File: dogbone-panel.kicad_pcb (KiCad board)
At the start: 2 copper layers, 35 x 60 mm, 72 parts, among them M1 THRU_HOLE_PAD, M10 THRU_HOLE_PAD, M11 THRU_HOLE_PAD, M12 THRU_HOLE_PAD, M2 THRU_HOLE_PAD, M3 THRU_HOLE_PAD, M4 THRU_HOLE_PAD, M5 THRU_HOLE_PAD, M6 THRU_HOLE_PAD, M7 THRU_HOLE_PAD, M8 THRU_HOLE_PAD, M9 THRU_HOLE_PAD

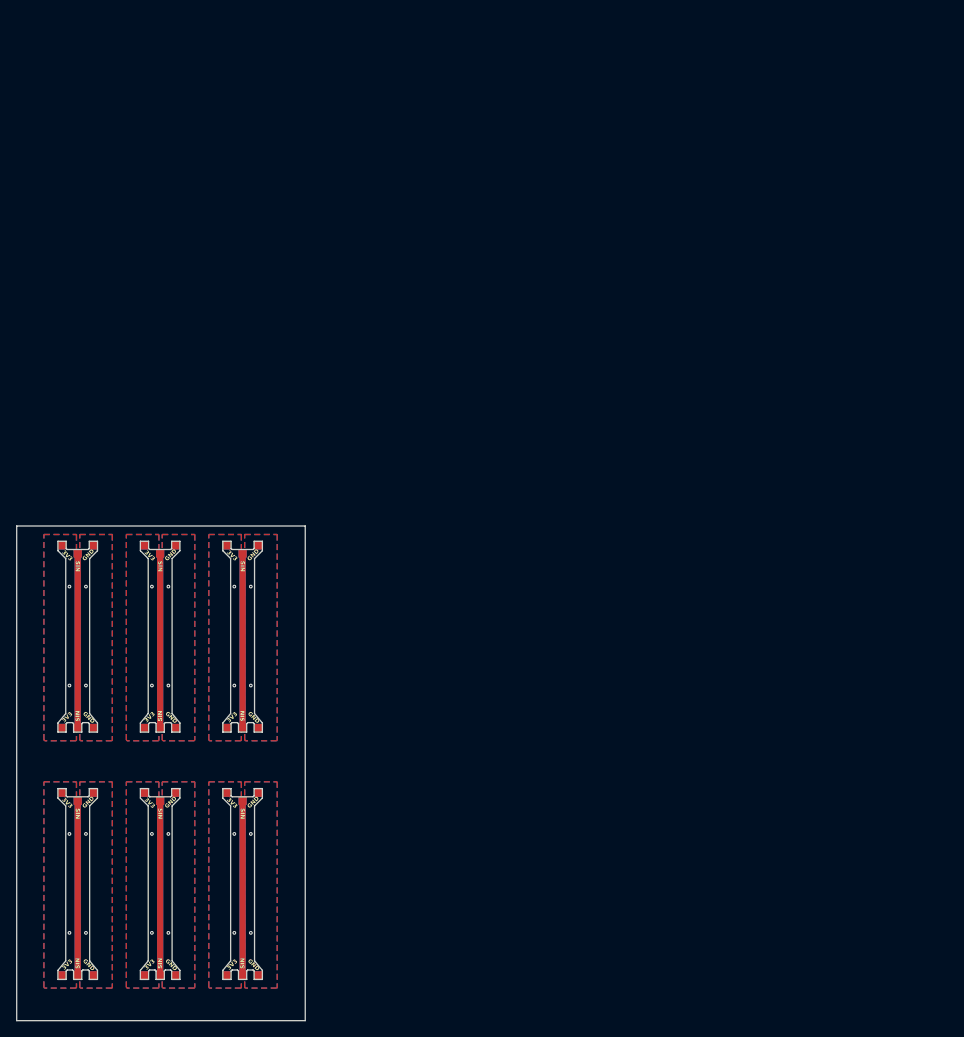
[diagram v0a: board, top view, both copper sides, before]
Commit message: board auto-panelized;
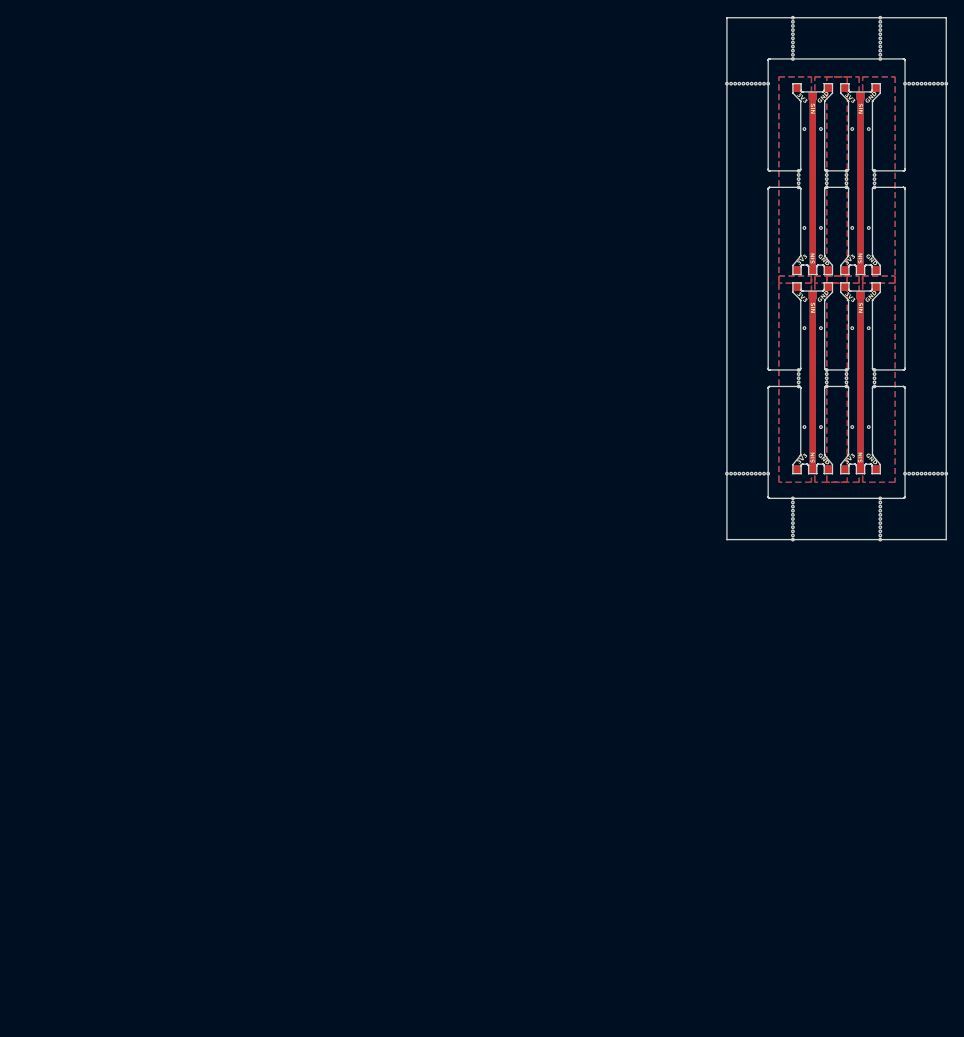
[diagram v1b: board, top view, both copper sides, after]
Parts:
- removed the M1 at (74.5, 84.0)
- removed the M1 at (54.5, 84.0)
- removed the M1 at (64.5, 114.0)
- removed the M1 at (64.5, 84.0)
- removed the M1 at (74.5, 114.0)
- removed the M1 at (54.5, 114.0)
- removed the M10 at (74.5, 106.2)
- removed the M10 at (54.5, 106.2)
- removed the M10 at (74.5, 136.2)
- removed the M10 at (64.5, 136.2)
- removed the M10 at (54.5, 136.2)
- removed the M10 at (64.5, 106.2)
- removed the M11 at (68.3, 136.2)
- removed the M11 at (78.3, 106.2)
- removed the M11 at (58.4, 106.2)
- removed the M11 at (68.3, 106.2)
- removed the M11 at (78.3, 136.2)
- removed the M11 at (58.4, 136.2)
- removed the M12 at (68.3, 106.2)
- removed the M12 at (78.3, 106.2)
- removed the M12 at (68.3, 136.2)
- removed the M12 at (78.3, 136.2)
- removed the M12 at (58.4, 106.2)
- removed the M12 at (58.4, 136.2)
- removed the M2 at (56.5, 106.2)
- removed the M2 at (66.5, 106.2)
- removed the M2 at (76.5, 136.2)
- removed the M2 at (76.5, 106.2)
- removed the M2 at (66.5, 136.2)
- removed the M2 at (56.5, 136.2)
- removed the M3 at (54.5, 136.2)
- removed the M3 at (74.5, 136.2)
- removed the M3 at (54.5, 106.2)
- removed the M3 at (74.5, 106.2)
- removed the M3 at (64.5, 106.2)
- removed the M3 at (64.5, 136.2)
- removed the M4 at (76.5, 85.0)
- removed the M4 at (76.5, 115.0)
- removed the M4 at (56.5, 115.0)
- removed the M4 at (66.5, 115.0)
- removed the M4 at (66.5, 85.0)
- removed the M4 at (56.5, 85.0)
- removed the M5 at (68.3, 114.0)
- removed the M5 at (68.3, 84.0)
- removed the M5 at (78.3, 114.0)
- removed the M5 at (58.4, 114.0)
- removed the M5 at (78.3, 84.0)
- removed the M5 at (58.4, 84.0)
- removed the M6 at (66.5, 136.2)
- removed the M6 at (76.5, 106.2)
- removed the M6 at (66.5, 106.2)
- removed the M6 at (56.5, 136.2)
- removed the M6 at (56.5, 106.2)
- removed the M6 at (76.5, 136.2)
- removed the M7 at (58.4, 114.0)
- removed the M7 at (58.4, 84.0)
- removed the M7 at (68.3, 114.0)
- removed the M7 at (68.3, 84.0)
- removed the M7 at (78.3, 84.0)
- removed the M7 at (78.3, 114.0)
- removed the M8 at (56.5, 115.0)
- removed the M8 at (76.5, 85.0)
- removed the M8 at (56.5, 85.0)
- removed the M8 at (66.5, 115.0)
- removed the M8 at (66.5, 85.0)
- removed the M8 at (76.5, 115.0)
- removed the M9 at (64.5, 114.0)
- removed the M9 at (64.5, 84.0)
- removed the M9 at (74.5, 84.0)
- removed the M9 at (74.5, 114.0)
- removed the M9 at (54.5, 84.0)
- removed the M9 at (54.5, 114.0)
- added KiKit_MB_10_10: NPTH, NPTH, F.Cu at (153.8, 24.0)
- added KiKit_MB_10_11: NPTH, NPTH, F.Cu at (153.8, 24.5)
- added KiKit_MB_10_12: NPTH, NPTH, F.Cu at (153.8, 25.0)
- added KiKit_MB_10_2: NPTH, NPTH, F.Cu at (153.8, 20.0)
- added KiKit_MB_10_3: NPTH, NPTH, F.Cu at (153.8, 20.5)
- added KiKit_MB_10_4: NPTH, NPTH, F.Cu at (153.8, 21.0)
- added KiKit_MB_10_5: NPTH, NPTH, F.Cu at (153.8, 21.5)
- added KiKit_MB_10_6: NPTH, NPTH, F.Cu at (153.8, 22.0)
- added KiKit_MB_10_7: NPTH, NPTH, F.Cu at (153.8, 22.5)
- added KiKit_MB_10_8: NPTH, NPTH, F.Cu at (153.8, 23.0)
- added KiKit_MB_10_9: NPTH, NPTH, F.Cu at (153.8, 23.5)
- added KiKit_MB_11_10: NPTH, NPTH, F.Cu at (143.2, 82.3)
- added KiKit_MB_11_11: NPTH, NPTH, F.Cu at (143.2, 82.8)
- added KiKit_MB_11_12: NPTH, NPTH, F.Cu at (143.2, 83.3)
- added KiKit_MB_11_2: NPTH, NPTH, F.Cu at (143.2, 78.3)
- added KiKit_MB_11_3: NPTH, NPTH, F.Cu at (143.2, 78.8)
- added KiKit_MB_11_4: NPTH, NPTH, F.Cu at (143.2, 79.3)
- added KiKit_MB_11_5: NPTH, NPTH, F.Cu at (143.2, 79.8)
- added KiKit_MB_11_6: NPTH, NPTH, F.Cu at (143.2, 80.3)
- added KiKit_MB_11_7: NPTH, NPTH, F.Cu at (143.2, 80.8)
- added KiKit_MB_11_8: NPTH, NPTH, F.Cu at (143.2, 81.3)
- added KiKit_MB_11_9: NPTH, NPTH, F.Cu at (143.2, 81.8)
- added KiKit_MB_12_10: NPTH, NPTH, F.Cu at (153.8, 82.3)
- added KiKit_MB_12_11: NPTH, NPTH, F.Cu at (153.8, 82.8)
- added KiKit_MB_12_12: NPTH, NPTH, F.Cu at (153.8, 83.3)
- added KiKit_MB_12_2: NPTH, NPTH, F.Cu at (153.8, 78.3)
- added KiKit_MB_12_3: NPTH, NPTH, F.Cu at (153.8, 78.8)
- added KiKit_MB_12_4: NPTH, NPTH, F.Cu at (153.8, 79.3)
- added KiKit_MB_12_5: NPTH, NPTH, F.Cu at (153.8, 79.8)
- added KiKit_MB_12_6: NPTH, NPTH, F.Cu at (153.8, 80.3)
- added KiKit_MB_12_7: NPTH, NPTH, F.Cu at (153.8, 80.8)
- added KiKit_MB_12_8: NPTH, NPTH, F.Cu at (153.8, 81.3)
- added KiKit_MB_12_9: NPTH, NPTH, F.Cu at (153.8, 81.8)
- added KiKit_MB_13_10: NPTH, NPTH, F.Cu at (139.2, 28.0)
- added KiKit_MB_13_11: NPTH, NPTH, F.Cu at (139.7, 28.0)
- added KiKit_MB_13_12: NPTH, NPTH, F.Cu at (140.2, 28.0)
- added KiKit_MB_13_2: NPTH, NPTH, F.Cu at (135.2, 28.0)
- added KiKit_MB_13_3: NPTH, NPTH, F.Cu at (135.7, 28.0)
- added KiKit_MB_13_4: NPTH, NPTH, F.Cu at (136.2, 28.0)
- added KiKit_MB_13_5: NPTH, NPTH, F.Cu at (136.7, 28.0)
- added KiKit_MB_13_6: NPTH, NPTH, F.Cu at (137.2, 28.0)
- added KiKit_MB_13_7: NPTH, NPTH, F.Cu at (137.7, 28.0)
- added KiKit_MB_13_8: NPTH, NPTH, F.Cu at (138.2, 28.0)
- added KiKit_MB_13_9: NPTH, NPTH, F.Cu at (138.7, 28.0)
- added KiKit_MB_14_10: NPTH, NPTH, F.Cu at (139.2, 75.3)
- added KiKit_MB_14_11: NPTH, NPTH, F.Cu at (139.7, 75.3)
- added KiKit_MB_14_12: NPTH, NPTH, F.Cu at (140.2, 75.3)
- added KiKit_MB_14_2: NPTH, NPTH, F.Cu at (135.2, 75.3)
- added KiKit_MB_14_3: NPTH, NPTH, F.Cu at (135.7, 75.3)
- added KiKit_MB_14_4: NPTH, NPTH, F.Cu at (136.2, 75.3)
- added KiKit_MB_14_5: NPTH, NPTH, F.Cu at (136.7, 75.3)
- added KiKit_MB_14_6: NPTH, NPTH, F.Cu at (137.2, 75.3)
- added KiKit_MB_14_7: NPTH, NPTH, F.Cu at (137.7, 75.3)
- added KiKit_MB_14_8: NPTH, NPTH, F.Cu at (138.2, 75.3)
- added KiKit_MB_14_9: NPTH, NPTH, F.Cu at (138.7, 75.3)
- added KiKit_MB_15_10: NPTH, NPTH, F.Cu at (160.8, 28.0)
- added KiKit_MB_15_11: NPTH, NPTH, F.Cu at (161.3, 28.0)
- added KiKit_MB_15_12: NPTH, NPTH, F.Cu at (161.8, 28.0)
- added KiKit_MB_15_2: NPTH, NPTH, F.Cu at (156.8, 28.0)
- added KiKit_MB_15_3: NPTH, NPTH, F.Cu at (157.3, 28.0)
- added KiKit_MB_15_4: NPTH, NPTH, F.Cu at (157.8, 28.0)
- added KiKit_MB_15_5: NPTH, NPTH, F.Cu at (158.3, 28.0)
- added KiKit_MB_15_6: NPTH, NPTH, F.Cu at (158.8, 28.0)
- added KiKit_MB_15_7: NPTH, NPTH, F.Cu at (159.3, 28.0)
- added KiKit_MB_15_8: NPTH, NPTH, F.Cu at (159.8, 28.0)
- added KiKit_MB_15_9: NPTH, NPTH, F.Cu at (160.3, 28.0)
- added KiKit_MB_16_10: NPTH, NPTH, F.Cu at (160.8, 75.3)
- added KiKit_MB_16_11: NPTH, NPTH, F.Cu at (161.3, 75.3)
- added KiKit_MB_16_12: NPTH, NPTH, F.Cu at (161.8, 75.3)
- added KiKit_MB_16_2: NPTH, NPTH, F.Cu at (156.8, 75.3)
- added KiKit_MB_16_3: NPTH, NPTH, F.Cu at (157.3, 75.3)
- added KiKit_MB_16_4: NPTH, NPTH, F.Cu at (157.8, 75.3)
- added KiKit_MB_16_5: NPTH, NPTH, F.Cu at (158.3, 75.3)
- added KiKit_MB_16_6: NPTH, NPTH, F.Cu at (158.8, 75.3)
- added KiKit_MB_16_7: NPTH, NPTH, F.Cu at (159.3, 75.3)
- added KiKit_MB_16_8: NPTH, NPTH, F.Cu at (159.8, 75.3)
- added KiKit_MB_16_9: NPTH, NPTH, F.Cu at (160.3, 75.3)
- added KiKit_MB_1_2: NPTH, NPTH, F.Cu at (143.9, 40.6)
- added KiKit_MB_1_3: NPTH, NPTH, F.Cu at (143.9, 40.1)
- added KiKit_MB_1_4: NPTH, NPTH, F.Cu at (143.9, 39.6)
- added KiKit_MB_1_5: NPTH, NPTH, F.Cu at (143.9, 39.1)
- added KiKit_MB_1_6: NPTH, NPTH, F.Cu at (143.9, 38.6)
- added KiKit_MB_2_2: NPTH, NPTH, F.Cu at (147.3, 38.6)
- added KiKit_MB_2_3: NPTH, NPTH, F.Cu at (147.3, 39.1)
- added KiKit_MB_2_4: NPTH, NPTH, F.Cu at (147.3, 39.6)
- added KiKit_MB_2_5: NPTH, NPTH, F.Cu at (147.3, 40.1)
- added KiKit_MB_2_6: NPTH, NPTH, F.Cu at (147.3, 40.6)
- added KiKit_MB_3_2: NPTH, NPTH, F.Cu at (149.7, 40.6)
- added KiKit_MB_3_3: NPTH, NPTH, F.Cu at (149.7, 40.1)
- added KiKit_MB_3_4: NPTH, NPTH, F.Cu at (149.7, 39.6)
- added KiKit_MB_3_5: NPTH, NPTH, F.Cu at (149.7, 39.1)
- added KiKit_MB_3_6: NPTH, NPTH, F.Cu at (149.7, 38.6)
- added KiKit_MB_4_2: NPTH, NPTH, F.Cu at (153.1, 38.6)
- added KiKit_MB_4_3: NPTH, NPTH, F.Cu at (153.1, 39.1)
- added KiKit_MB_4_4: NPTH, NPTH, F.Cu at (153.1, 39.6)
- added KiKit_MB_4_5: NPTH, NPTH, F.Cu at (153.1, 40.1)
- added KiKit_MB_4_6: NPTH, NPTH, F.Cu at (153.1, 40.6)
- added KiKit_MB_5_2: NPTH, NPTH, F.Cu at (143.9, 64.7)
- added KiKit_MB_5_3: NPTH, NPTH, F.Cu at (143.9, 64.2)
- added KiKit_MB_5_4: NPTH, NPTH, F.Cu at (143.9, 63.7)
- added KiKit_MB_5_5: NPTH, NPTH, F.Cu at (143.9, 63.2)
- added KiKit_MB_5_6: NPTH, NPTH, F.Cu at (143.9, 62.7)
- added KiKit_MB_6_2: NPTH, NPTH, F.Cu at (147.3, 62.7)
- added KiKit_MB_6_3: NPTH, NPTH, F.Cu at (147.3, 63.2)
- added KiKit_MB_6_4: NPTH, NPTH, F.Cu at (147.3, 63.7)
- added KiKit_MB_6_5: NPTH, NPTH, F.Cu at (147.3, 64.2)
- added KiKit_MB_6_6: NPTH, NPTH, F.Cu at (147.3, 64.7)
- added KiKit_MB_7_2: NPTH, NPTH, F.Cu at (149.7, 64.7)
- added KiKit_MB_7_3: NPTH, NPTH, F.Cu at (149.7, 64.2)
- added KiKit_MB_7_4: NPTH, NPTH, F.Cu at (149.7, 63.7)
- added KiKit_MB_7_5: NPTH, NPTH, F.Cu at (149.7, 63.2)
- added KiKit_MB_7_6: NPTH, NPTH, F.Cu at (149.7, 62.7)
- added KiKit_MB_8_2: NPTH, NPTH, F.Cu at (153.1, 62.7)
- added KiKit_MB_8_3: NPTH, NPTH, F.Cu at (153.1, 63.2)
- added KiKit_MB_8_4: NPTH, NPTH, F.Cu at (153.1, 63.7)
- added KiKit_MB_8_5: NPTH, NPTH, F.Cu at (153.1, 64.2)
- added KiKit_MB_8_6: NPTH, NPTH, F.Cu at (153.1, 64.7)
- added KiKit_MB_9_10: NPTH, NPTH, F.Cu at (143.2, 24.0)
- added KiKit_MB_9_11: NPTH, NPTH, F.Cu at (143.2, 24.5)
- added KiKit_MB_9_12: NPTH, NPTH, F.Cu at (143.2, 25.0)
- added KiKit_MB_9_2: NPTH, NPTH, F.Cu at (143.2, 20.0)
- added KiKit_MB_9_3: NPTH, NPTH, F.Cu at (143.2, 20.5)
- added KiKit_MB_9_4: NPTH, NPTH, F.Cu at (143.2, 21.0)
- added KiKit_MB_9_5: NPTH, NPTH, F.Cu at (143.2, 21.5)
- added KiKit_MB_9_6: NPTH, NPTH, F.Cu at (143.2, 22.0)
- added KiKit_MB_9_7: NPTH, NPTH, F.Cu at (143.2, 22.5)
- added KiKit_MB_9_8: NPTH, NPTH, F.Cu at (143.2, 23.0)
- added KiKit_MB_9_9: NPTH, NPTH, F.Cu at (143.2, 23.5)
- added M1: THRU_HOLE_PAD, adapter-encoder:dogbone_pad, F.Cu at (143.7, 52.6)
- added M1: THRU_HOLE_PAD, adapter-encoder:dogbone_pad, F.Cu at (149.5, 28.5)
- added M1: THRU_HOLE_PAD, adapter-encoder:dogbone_pad, F.Cu at (143.7, 28.5)
- added M1: THRU_HOLE_PAD, adapter-encoder:dogbone_pad, F.Cu at (149.5, 52.6)
- added M10: THRU_HOLE_PAD, adapter-encoder:dogbone_pad, B.Cu at (149.5, 74.8)
- added M10: THRU_HOLE_PAD, adapter-encoder:dogbone_pad, B.Cu at (143.7, 50.6)
- added M10: THRU_HOLE_PAD, adapter-encoder:dogbone_pad, B.Cu at (149.5, 50.6)
- added M10: THRU_HOLE_PAD, adapter-encoder:dogbone_pad, B.Cu at (143.7, 74.8)
- added M11: THRU_HOLE_PAD, adapter-encoder:dogbone_pad, F.Cu at (147.5, 50.6)
- added M11: THRU_HOLE_PAD, adapter-encoder:dogbone_pad, F.Cu at (147.5, 74.8)
- added M11: THRU_HOLE_PAD, adapter-encoder:dogbone_pad, F.Cu at (153.3, 74.8)
- added M11: THRU_HOLE_PAD, adapter-encoder:dogbone_pad, F.Cu at (153.3, 50.6)
- added M12: THRU_HOLE_PAD, adapter-encoder:dogbone_pad, B.Cu at (153.3, 74.8)
- added M12: THRU_HOLE_PAD, adapter-encoder:dogbone_pad, B.Cu at (153.3, 50.6)
- added M12: THRU_HOLE_PAD, adapter-encoder:dogbone_pad, B.Cu at (147.5, 74.8)
- added M12: THRU_HOLE_PAD, adapter-encoder:dogbone_pad, B.Cu at (147.5, 50.6)
- added M2: THRU_HOLE_PAD, adapter-encoder:dogbone_pad, F.Cu at (145.6, 50.6)
- added M2: THRU_HOLE_PAD, adapter-encoder:dogbone_pad, F.Cu at (151.4, 74.8)
- added M2: THRU_HOLE_PAD, adapter-encoder:dogbone_pad, F.Cu at (151.4, 50.6)
- added M2: THRU_HOLE_PAD, adapter-encoder:dogbone_pad, F.Cu at (145.6, 74.8)
- added M3: THRU_HOLE_PAD, adapter-encoder:dogbone_pad, F.Cu at (143.7, 50.6)
- added M3: THRU_HOLE_PAD, adapter-encoder:dogbone_pad, F.Cu at (149.5, 50.6)
- added M3: THRU_HOLE_PAD, adapter-encoder:dogbone_pad, F.Cu at (149.5, 74.8)
- added M3: THRU_HOLE_PAD, adapter-encoder:dogbone_pad, F.Cu at (143.7, 74.8)
- added M4: THRU_HOLE_PAD, adapter-encoder:dogbone_pad, F.Cu at (151.4, 53.6)
- added M4: THRU_HOLE_PAD, adapter-encoder:dogbone_pad, F.Cu at (145.6, 29.5)
- added M4: THRU_HOLE_PAD, adapter-encoder:dogbone_pad, F.Cu at (145.6, 53.6)
- added M4: THRU_HOLE_PAD, adapter-encoder:dogbone_pad, F.Cu at (151.4, 29.5)
- added M5: THRU_HOLE_PAD, adapter-encoder:dogbone_pad, F.Cu at (147.5, 28.5)
- added M5: THRU_HOLE_PAD, adapter-encoder:dogbone_pad, F.Cu at (147.5, 52.6)
- added M5: THRU_HOLE_PAD, adapter-encoder:dogbone_pad, F.Cu at (153.3, 52.6)
- added M5: THRU_HOLE_PAD, adapter-encoder:dogbone_pad, F.Cu at (153.3, 28.5)
- added M6: THRU_HOLE_PAD, adapter-encoder:dogbone_pad, B.Cu at (145.6, 50.6)
- added M6: THRU_HOLE_PAD, adapter-encoder:dogbone_pad, B.Cu at (151.4, 74.8)
- added M6: THRU_HOLE_PAD, adapter-encoder:dogbone_pad, B.Cu at (145.6, 74.8)
- added M6: THRU_HOLE_PAD, adapter-encoder:dogbone_pad, B.Cu at (151.4, 50.6)
- added M7: THRU_HOLE_PAD, adapter-encoder:dogbone_pad, B.Cu at (153.3, 28.5)
- added M7: THRU_HOLE_PAD, adapter-encoder:dogbone_pad, B.Cu at (147.5, 28.5)
- added M7: THRU_HOLE_PAD, adapter-encoder:dogbone_pad, B.Cu at (147.5, 52.6)
- added M7: THRU_HOLE_PAD, adapter-encoder:dogbone_pad, B.Cu at (153.3, 52.6)
- added M8: THRU_HOLE_PAD, adapter-encoder:dogbone_pad, B.Cu at (145.6, 29.5)
- added M8: THRU_HOLE_PAD, adapter-encoder:dogbone_pad, B.Cu at (151.4, 29.5)
- added M8: THRU_HOLE_PAD, adapter-encoder:dogbone_pad, B.Cu at (145.6, 53.6)
- added M8: THRU_HOLE_PAD, adapter-encoder:dogbone_pad, B.Cu at (151.4, 53.6)
- added M9: THRU_HOLE_PAD, adapter-encoder:dogbone_pad, B.Cu at (143.7, 52.6)
- added M9: THRU_HOLE_PAD, adapter-encoder:dogbone_pad, B.Cu at (143.7, 28.5)
- added M9: THRU_HOLE_PAD, adapter-encoder:dogbone_pad, B.Cu at (149.5, 28.5)
- added M9: THRU_HOLE_PAD, adapter-encoder:dogbone_pad, B.Cu at (149.5, 52.6)
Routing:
- net /SIN: track 126.9 -> 0.00 mm
- net /COS: track 126.9 -> 0.00 mm
- net Board_3-/SIN: track 0.00 -> 21.1 mm
- net Board_3-/COS: track 0.00 -> 21.1 mm
- net Board_2-/SIN: track 0.00 -> 21.1 mm
- net Board_2-/COS: track 0.00 -> 21.1 mm
- net Board_1-/SIN: track 0.00 -> 21.1 mm
- net Board_1-/COS: track 0.00 -> 21.1 mm
- net Board_0-/SIN: track 0.00 -> 21.1 mm
- net Board_0-/COS: track 0.00 -> 21.1 mm
- net Board_3-/GND: vias 0 -> 2
- net Board_3-/+3V3: vias 0 -> 2
- net Board_2-/GND: vias 0 -> 2
- net Board_2-/+3V3: vias 0 -> 2
- net Board_1-/GND: vias 0 -> 2
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- added copper zone on B.Cu, net Board_0-/+3V3
- added copper zone on F.Cu, net Board_0-/+3V3
- added copper zone on B.Cu, net Board_0-/GND
- added copper zone on F.Cu, net Board_0-/GND
- added copper zone on B.Cu, net Board_1-/+3V3
- added copper zone on F.Cu, net Board_1-/+3V3
- added copper zone on B.Cu, net Board_1-/GND
- added copper zone on F.Cu, net Board_1-/GND
- added copper zone on B.Cu, net Board_2-/+3V3
- added copper zone on F.Cu, net Board_2-/+3V3
- added copper zone on B.Cu, net Board_2-/GND
- added copper zone on F.Cu, net Board_2-/GND
- added copper zone on B.Cu, net Board_3-/+3V3
- added copper zone on F.Cu, net Board_3-/+3V3
- added copper zone on B.Cu, net Board_3-/GND
- added copper zone on F.Cu, net Board_3-/GND
- removed copper zone on B.Cu, net /+3V3
- removed copper zone on F.Cu, net /+3V3
- removed copper zone on B.Cu, net /GND
- removed copper zone on F.Cu, net /GND
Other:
- board size 35 x 60 mm -> 26.6 x 63.3 mm

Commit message: panelization options
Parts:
- removed KiKit_MB_10_10, KiKit_MB_10_11, KiKit_MB_10_12, KiKit_MB_10_2, KiKit_MB_10_3, KiKit_MB_10_4, KiKit_MB_10_5, KiKit_MB_10_6, KiKit_MB_10_7, KiKit_MB_10_8, KiKit_MB_10_9, KiKit_MB_11_10, KiKit_MB_11_11, KiKit_MB_11_12, KiKit_MB_11_2, KiKit_MB_11_3, KiKit_MB_11_4, KiKit_MB_11_5, KiKit_MB_11_6, KiKit_MB_11_7, KiKit_MB_11_8, KiKit_MB_11_9, KiKit_MB_12_10, KiKit_MB_12_11, KiKit_MB_12_12, KiKit_MB_12_2, KiKit_MB_12_3, KiKit_MB_12_4, KiKit_MB_12_5, KiKit_MB_12_6, KiKit_MB_12_7, KiKit_MB_12_8, KiKit_MB_12_9, KiKit_MB_13_10, KiKit_MB_13_11, KiKit_MB_13_12, KiKit_MB_13_2, KiKit_MB_13_3, KiKit_MB_13_4, KiKit_MB_13_5, KiKit_MB_13_6, KiKit_MB_13_7, KiKit_MB_13_8, KiKit_MB_13_9, KiKit_MB_14_10, KiKit_MB_14_11, KiKit_MB_14_12, KiKit_MB_14_2, KiKit_MB_14_3, KiKit_MB_14_4, KiKit_MB_14_5, KiKit_MB_14_6, KiKit_MB_14_7, KiKit_MB_14_8, KiKit_MB_14_9, KiKit_MB_15_10, KiKit_MB_15_11, KiKit_MB_15_12, KiKit_MB_15_2, KiKit_MB_15_3, KiKit_MB_15_4, KiKit_MB_15_5, KiKit_MB_15_6, KiKit_MB_15_7, KiKit_MB_15_8, KiKit_MB_15_9, KiKit_MB_16_10, KiKit_MB_16_11, KiKit_MB_16_12, KiKit_MB_16_2, KiKit_MB_16_3, KiKit_MB_16_4, KiKit_MB_16_5, KiKit_MB_16_6, KiKit_MB_16_7, KiKit_MB_16_8, KiKit_MB_16_9, KiKit_MB_9_10, KiKit_MB_9_11, KiKit_MB_9_12, KiKit_MB_9_2, KiKit_MB_9_3, KiKit_MB_9_4, KiKit_MB_9_5, KiKit_MB_9_6, KiKit_MB_9_7, KiKit_MB_9_8, KiKit_MB_9_9: NPTH, NPTH
- removed the M1 at (143.7, 52.6)
- removed the M1 at (149.5, 28.5)
- removed the M1 at (143.7, 28.5)
- removed the M1 at (149.5, 52.6)
- removed the M10 at (149.5, 74.8)
- removed the M10 at (143.7, 50.6)
- removed the M10 at (149.5, 50.6)
- removed the M10 at (143.7, 74.8)
- removed the M11 at (147.5, 50.6)
- removed the M11 at (147.5, 74.8)
- removed the M11 at (153.3, 74.8)
- removed the M11 at (153.3, 50.6)
- removed the M12 at (153.3, 74.8)
- removed the M12 at (153.3, 50.6)
- removed the M12 at (147.5, 74.8)
- removed the M12 at (147.5, 50.6)
- removed the M2 at (145.6, 50.6)
- removed the M2 at (151.4, 74.8)
- removed the M2 at (151.4, 50.6)
- removed the M2 at (145.6, 74.8)
- removed the M3 at (143.7, 50.6)
- removed the M3 at (149.5, 50.6)
- removed the M3 at (149.5, 74.8)
- removed the M3 at (143.7, 74.8)
- removed the M4 at (151.4, 53.6)
- removed the M4 at (145.6, 29.5)
- removed the M4 at (145.6, 53.6)
- removed the M4 at (151.4, 29.5)
- removed the M5 at (147.5, 28.5)
- removed the M5 at (147.5, 52.6)
- removed the M5 at (153.3, 52.6)
- removed the M5 at (153.3, 28.5)
- removed the M6 at (145.6, 50.6)
- removed the M6 at (151.4, 74.8)
- removed the M6 at (145.6, 74.8)
- removed the M6 at (151.4, 50.6)
- removed the M7 at (153.3, 28.5)
- removed the M7 at (147.5, 28.5)
- removed the M7 at (147.5, 52.6)
- removed the M7 at (153.3, 52.6)
- removed the M8 at (145.6, 29.5)
- removed the M8 at (151.4, 29.5)
- removed the M8 at (145.6, 53.6)
- removed the M8 at (151.4, 53.6)
- removed the M9 at (143.7, 52.6)
- removed the M9 at (143.7, 28.5)
- removed the M9 at (149.5, 28.5)
- removed the M9 at (149.5, 52.6)
- added KiKit_MB_1_7: NPTH, NPTH, F.Cu at (143.9, 36.6)
- added KiKit_MB_1_8: NPTH, NPTH, F.Cu at (143.9, 36.1)
- added KiKit_MB_2_7: NPTH, NPTH, F.Cu at (147.3, 38.6)
- added KiKit_MB_2_8: NPTH, NPTH, F.Cu at (147.3, 39.1)
- added KiKit_MB_3_7: NPTH, NPTH, F.Cu at (149.7, 36.6)
- added KiKit_MB_3_8: NPTH, NPTH, F.Cu at (149.7, 36.1)
- added KiKit_MB_4_7: NPTH, NPTH, F.Cu at (153.1, 38.6)
- added KiKit_MB_4_8: NPTH, NPTH, F.Cu at (153.1, 39.1)
- added KiKit_MB_5_7: NPTH, NPTH, F.Cu at (143.9, 60.7)
- added KiKit_MB_5_8: NPTH, NPTH, F.Cu at (143.9, 60.2)
- added KiKit_MB_6_7: NPTH, NPTH, F.Cu at (147.3, 62.7)
- added KiKit_MB_6_8: NPTH, NPTH, F.Cu at (147.3, 63.2)
- added KiKit_MB_7_7: NPTH, NPTH, F.Cu at (149.7, 60.7)
- added KiKit_MB_7_8: NPTH, NPTH, F.Cu at (149.7, 60.2)
- added KiKit_MB_8_7: NPTH, NPTH, F.Cu at (153.1, 62.7)
- added KiKit_MB_8_8: NPTH, NPTH, F.Cu at (153.1, 63.2)
- added M1: THRU_HOLE_PAD, adapter-encoder:dogbone_pad, F.Cu at (149.5, 26.5)
- added M1: THRU_HOLE_PAD, adapter-encoder:dogbone_pad, F.Cu at (143.7, 26.5)
- added M1: THRU_HOLE_PAD, adapter-encoder:dogbone_pad, F.Cu at (143.7, 50.6)
- added M1: THRU_HOLE_PAD, adapter-encoder:dogbone_pad, F.Cu at (149.5, 50.6)
- added M10: THRU_HOLE_PAD, adapter-encoder:dogbone_pad, B.Cu at (149.5, 48.6)
- added M10: THRU_HOLE_PAD, adapter-encoder:dogbone_pad, B.Cu at (143.7, 48.6)
- added M10: THRU_HOLE_PAD, adapter-encoder:dogbone_pad, B.Cu at (149.5, 72.8)
- added M10: THRU_HOLE_PAD, adapter-encoder:dogbone_pad, B.Cu at (143.7, 72.8)
- added M11: THRU_HOLE_PAD, adapter-encoder:dogbone_pad, F.Cu at (153.3, 72.8)
- added M11: THRU_HOLE_PAD, adapter-encoder:dogbone_pad, F.Cu at (147.5, 72.8)
- added M11: THRU_HOLE_PAD, adapter-encoder:dogbone_pad, F.Cu at (147.5, 48.6)
- added M11: THRU_HOLE_PAD, adapter-encoder:dogbone_pad, F.Cu at (153.3, 48.6)
- added M12: THRU_HOLE_PAD, adapter-encoder:dogbone_pad, B.Cu at (153.3, 48.6)
- added M12: THRU_HOLE_PAD, adapter-encoder:dogbone_pad, B.Cu at (147.5, 48.6)
- added M12: THRU_HOLE_PAD, adapter-encoder:dogbone_pad, B.Cu at (153.3, 72.8)
- added M12: THRU_HOLE_PAD, adapter-encoder:dogbone_pad, B.Cu at (147.5, 72.8)
- added M2: THRU_HOLE_PAD, adapter-encoder:dogbone_pad, F.Cu at (145.6, 48.6)
- added M2: THRU_HOLE_PAD, adapter-encoder:dogbone_pad, F.Cu at (151.4, 48.6)
- added M2: THRU_HOLE_PAD, adapter-encoder:dogbone_pad, F.Cu at (145.6, 72.8)
- added M2: THRU_HOLE_PAD, adapter-encoder:dogbone_pad, F.Cu at (151.4, 72.8)
- added M3: THRU_HOLE_PAD, adapter-encoder:dogbone_pad, F.Cu at (143.7, 72.8)
- added M3: THRU_HOLE_PAD, adapter-encoder:dogbone_pad, F.Cu at (143.7, 48.6)
- added M3: THRU_HOLE_PAD, adapter-encoder:dogbone_pad, F.Cu at (149.5, 48.6)
- added M3: THRU_HOLE_PAD, adapter-encoder:dogbone_pad, F.Cu at (149.5, 72.8)
- added M4: THRU_HOLE_PAD, adapter-encoder:dogbone_pad, F.Cu at (151.4, 51.6)
- added M4: THRU_HOLE_PAD, adapter-encoder:dogbone_pad, F.Cu at (145.6, 51.6)
- added M4: THRU_HOLE_PAD, adapter-encoder:dogbone_pad, F.Cu at (151.4, 27.5)
- added M4: THRU_HOLE_PAD, adapter-encoder:dogbone_pad, F.Cu at (145.6, 27.5)
- added M5: THRU_HOLE_PAD, adapter-encoder:dogbone_pad, F.Cu at (153.3, 26.5)
- added M5: THRU_HOLE_PAD, adapter-encoder:dogbone_pad, F.Cu at (147.5, 26.5)
- added M5: THRU_HOLE_PAD, adapter-encoder:dogbone_pad, F.Cu at (147.5, 50.6)
- added M5: THRU_HOLE_PAD, adapter-encoder:dogbone_pad, F.Cu at (153.3, 50.6)
- added M6: THRU_HOLE_PAD, adapter-encoder:dogbone_pad, B.Cu at (145.6, 72.8)
- added M6: THRU_HOLE_PAD, adapter-encoder:dogbone_pad, B.Cu at (151.4, 72.8)
- added M6: THRU_HOLE_PAD, adapter-encoder:dogbone_pad, B.Cu at (151.4, 48.6)
- added M6: THRU_HOLE_PAD, adapter-encoder:dogbone_pad, B.Cu at (145.6, 48.6)
- added M7: THRU_HOLE_PAD, adapter-encoder:dogbone_pad, B.Cu at (153.3, 50.6)
- added M7: THRU_HOLE_PAD, adapter-encoder:dogbone_pad, B.Cu at (147.5, 26.5)
- added M7: THRU_HOLE_PAD, adapter-encoder:dogbone_pad, B.Cu at (153.3, 26.5)
- added M7: THRU_HOLE_PAD, adapter-encoder:dogbone_pad, B.Cu at (147.5, 50.6)
- added M8: THRU_HOLE_PAD, adapter-encoder:dogbone_pad, B.Cu at (145.6, 27.5)
- added M8: THRU_HOLE_PAD, adapter-encoder:dogbone_pad, B.Cu at (151.4, 51.6)
- added M8: THRU_HOLE_PAD, adapter-encoder:dogbone_pad, B.Cu at (151.4, 27.5)
- added M8: THRU_HOLE_PAD, adapter-encoder:dogbone_pad, B.Cu at (145.6, 51.6)
- added M9: THRU_HOLE_PAD, adapter-encoder:dogbone_pad, B.Cu at (143.7, 26.5)
- added M9: THRU_HOLE_PAD, adapter-encoder:dogbone_pad, B.Cu at (149.5, 26.5)
- added M9: THRU_HOLE_PAD, adapter-encoder:dogbone_pad, B.Cu at (149.5, 50.6)
- added M9: THRU_HOLE_PAD, adapter-encoder:dogbone_pad, B.Cu at (143.7, 50.6)
- moved KiKit_MB_2_2 2.50 mm to (147.3, 36.1)
- moved KiKit_MB_2_3 2.50 mm to (147.3, 36.6)
- moved KiKit_MB_2_4 2.50 mm to (147.3, 37.1)
- moved KiKit_MB_2_5 2.50 mm to (147.3, 37.6)
- moved KiKit_MB_2_6 2.50 mm to (147.3, 38.1)
- moved KiKit_MB_4_2 2.50 mm to (153.1, 36.1)
- moved KiKit_MB_4_3 2.50 mm to (153.1, 36.6)
- moved KiKit_MB_4_4 2.50 mm to (153.1, 37.1)
- moved KiKit_MB_4_5 2.50 mm to (153.1, 37.6)
- moved KiKit_MB_4_6 2.50 mm to (153.1, 38.1)
- moved KiKit_MB_6_2 2.50 mm to (147.3, 60.2)
- moved KiKit_MB_6_3 2.50 mm to (147.3, 60.7)
- moved KiKit_MB_6_4 2.50 mm to (147.3, 61.2)
- moved KiKit_MB_8_2 2.50 mm to (153.1, 60.2)
- moved KiKit_MB_8_3 2.50 mm to (153.1, 60.7)
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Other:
- board size 26.6 x 63.3 mm -> 22.6 x 59.3 mm
